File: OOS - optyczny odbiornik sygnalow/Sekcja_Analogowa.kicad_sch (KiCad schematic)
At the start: 52 parts, among them J1 Conn_01x02_Socket, J2 Conn_01x02_Socket, J3 Conn_01x02_Socket, J4 Conn_01x02_Socket, J5 Conn_Coaxial, U1 OPA300AIDBVR, U2 OPA300AIDBVR

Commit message: Finish Li-Lion section, add for review
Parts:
- removed D1, D2: LED, Diode_SMD:D_0603_1608Metric_Pad1.05x0.95mm_HandSolder, symbol Device:LED
- removed J1, J2, J3: Conn_01x02_Socket, Connector_PinHeader_2.54mm:PinHeader_1x02_P2.54mm_Vertical, symbol Connector:Conn_01x02_Socket
- removed R1: 10k, Resistor_SMD:R_0603_1608Metric_Pad0.98x0.95mm_HandSolder, symbol Device:R
- removed R2: 2k2, Resistor_SMD:R_0603_1608Metric_Pad0.98x0.95mm_HandSolder, symbol Device:R
- added TP34: TestPoint_Small, TestPoint:TestPoint_Pad_D1.0mm, symbol Connector:TestPoint_Small
- JP1: footprint Jumper:SolderJumper-2_P1.3mm_Bridged_RoundedPad1.0x1.5mm -> Jumper:SolderJumper-2_P1.3mm_Open_RoundedPad1.0x1.5mm
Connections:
- net U1/U2_En_Alt_Con: now also TP34.1
- net +5V renamed +3V3
- net +V_photo renamed +32V
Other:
- note added: "1V1"
- note added: "2V2"
- note added: "For U1_Out(max) = 10uA(Imax) * 1kR(Rf) = 10mV @ 10uA"
- note added: "Inverting amplifier x10 (1k/100)"
- note added: "changed from short to open"
- note added: "changed position 0V on schematic"
- note added: "changed value to be hidden"
- note added: "removed connectors for +V_photo, +5V and GND"
- note added: "removed indication diode from sekcja analogowa to dcdc boost"
- note removed: "+V_photo 5V to 32V"
- note removed: "1V66"
- note removed: "3V33"
- note removed: "Inverting amplifier x10 (10k/1k)"
- moved on the sheet: C1, C10, C11, C12, C2, C3, C4, C5, C6, C7, C8, C9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

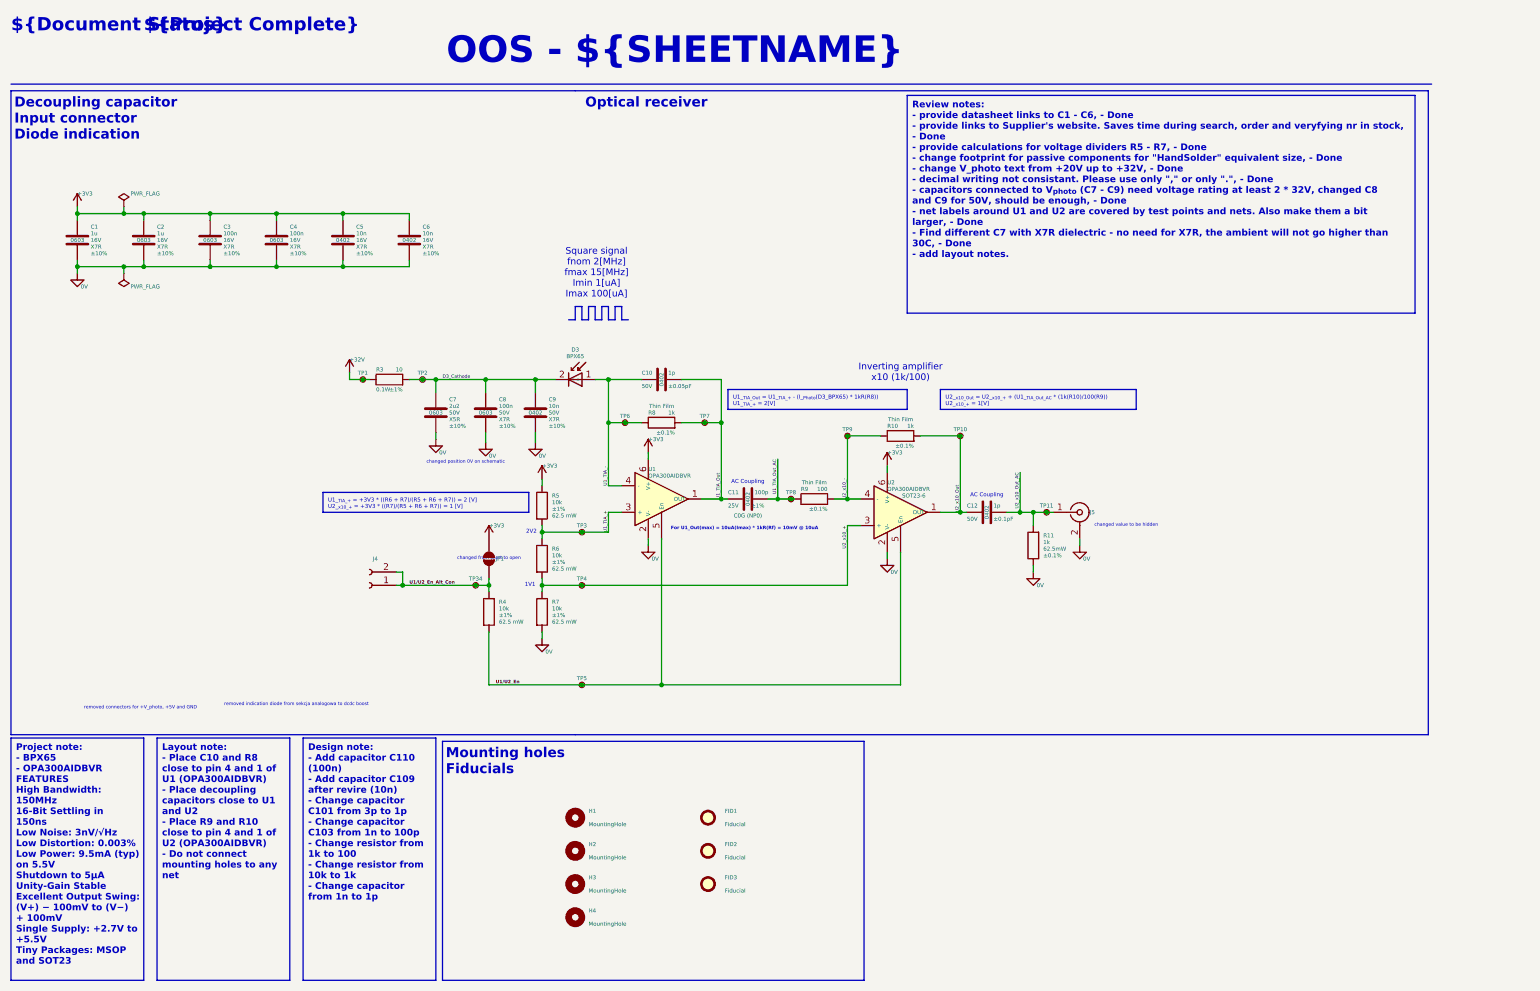
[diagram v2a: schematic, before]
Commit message: Implementing changes after review on Li-Ion section, adding components to USB section
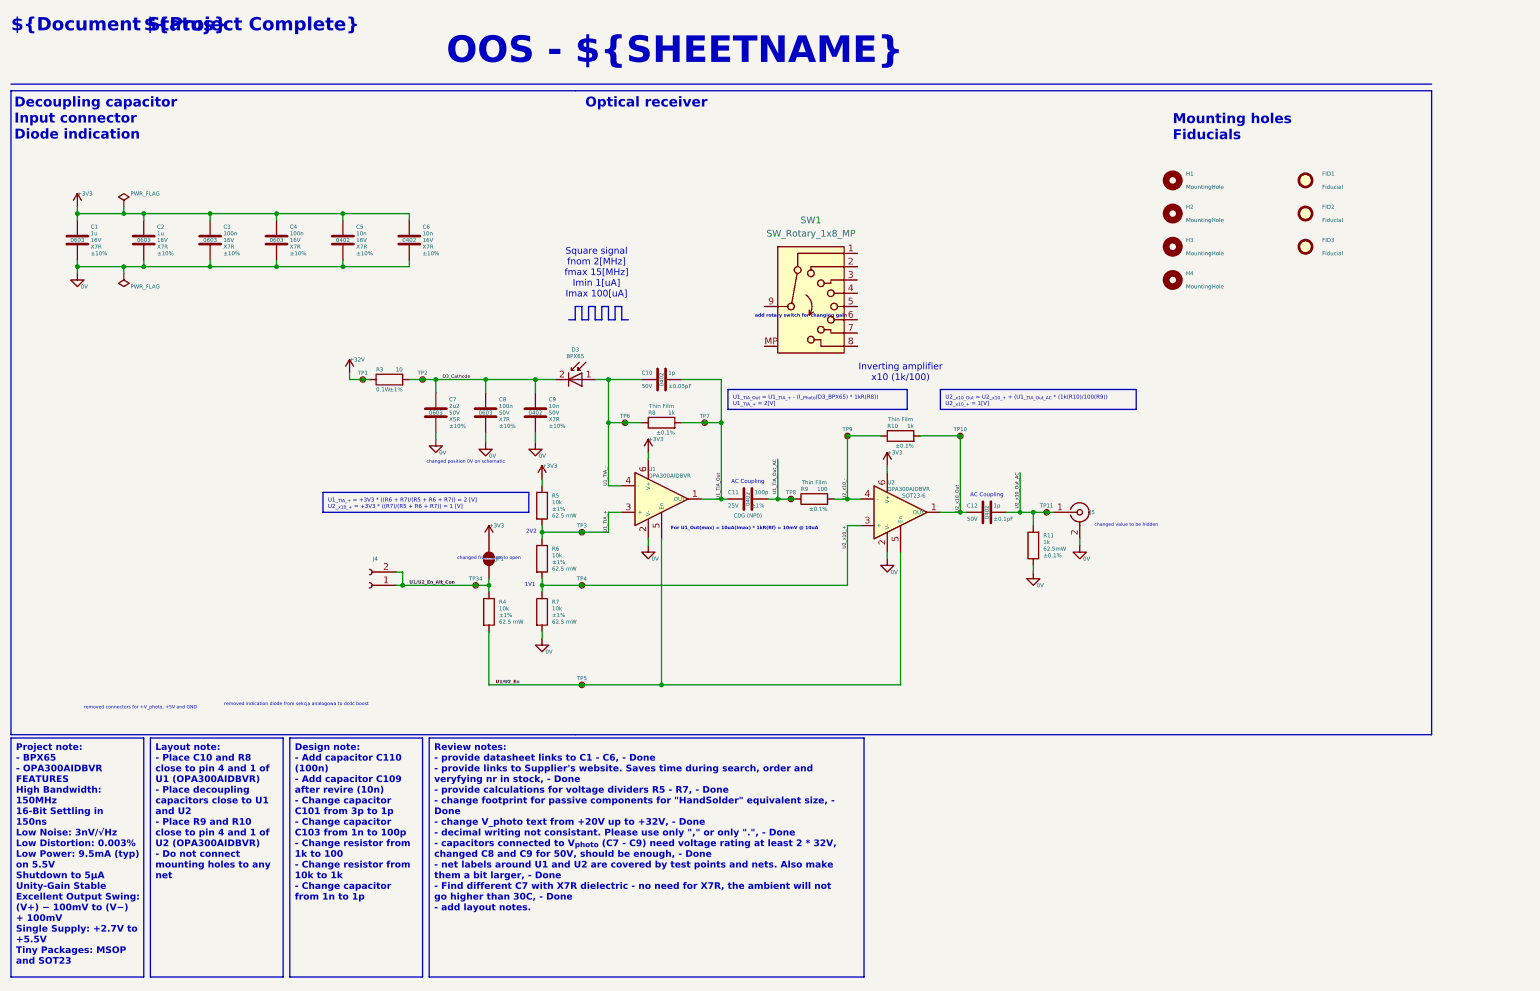
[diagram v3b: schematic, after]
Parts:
- added SW1: SW_Rotary_1x8_MP, Button_Switch_SMD:Nidec_Copal_SH-7040B, symbol Switch:SW_Rotary_1x8_MP
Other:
- note added: "add rotary switch for changing gain"
- moved on the sheet: FID1, FID2, FID3, H1, H2, H3, H4

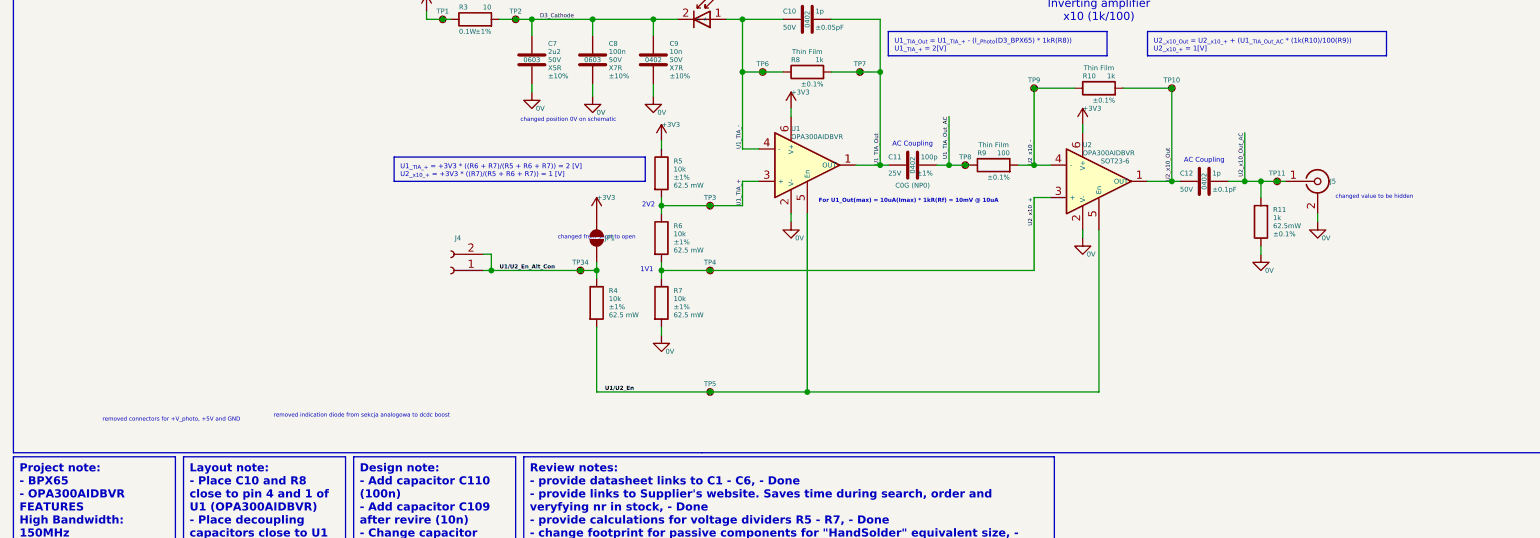
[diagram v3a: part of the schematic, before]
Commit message: Clean schematic, what left is to add resistors for pull down on usb page and rotary switch on analog page
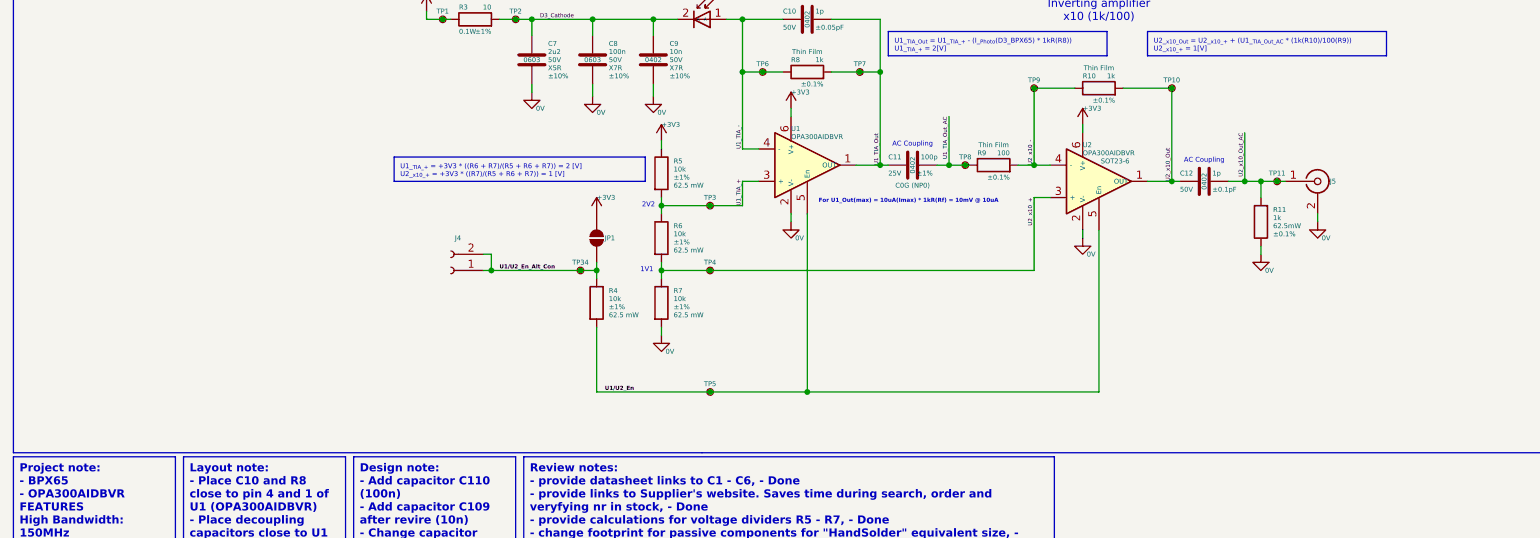
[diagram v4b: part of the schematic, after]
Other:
- note removed: "changed from short to open"
- note removed: "changed position 0V on schematic"
- note removed: "changed value to be hidden"
- note removed: "removed connectors for +V_photo, +5V and GND"
- note removed: "removed indication diode from sekcja analogowa to dcdc boost"
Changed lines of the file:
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@@
 		(comment 4 "${Project Reason}")
-	)
-	(text "removed indication diode from sekcja analogowa to dcdc boost"
-		(exclude_from_sim no)
-		(at 67.31 144.78 0)
-		(effects
-			(font
-				(size 0.635 0.635)
-				(color 255 0 0 1)
-			)
-		)
 	)
 	(text "Square signal\nfnom 2[MHz]\nfmax 15[MHz]\nImin 1[uA]\nImax 100[uA]"
@@
 				(bold yes)
 				(color 132 132 0 1)
-			)
-		)
-	)
-	(text "changed from short to open"
-		(exclude_from_sim no)
-		(at 104.14 116.84 0)
-		(effects
-			(font
-				(size 0.635 0.635)
-				(color 255 0 0 1)
 			)
 		)
@@
 		)
 	)
-	(text "changed value to be hidden"
-		(exclude_from_sim no)
-		(at 226.06 110.49 0)
-		(effects
-			(font
-				(size 0.635 0.635)
-				(color 255 0 0 1)
-			)
-		)
-	)
 	(text "${Document Status}"
 		(exclude_from_sim no)
@@
 		)
 	)
-	(text "changed position 0V on schematic"
-		(exclude_from_sim no)
-		(at 99.695 98.425 0)
-		(effects
-			(font
-				(size 0.635 0.635)
-				(color 255 0 0 1)
-			)
-		)
-	)
 	(text "2V2"
 		(exclude_from_sim no)
@@
 		)
 	)
-	(text "removed connectors for +V_photo, +5V and GND"
-		(exclude_from_sim no)
-		(at 37.465 145.415 0)
-		(effects
-			(font
-				(size 0.635 0.635)
-				(color 255 0 0 1)
-			)
-		)
-	)

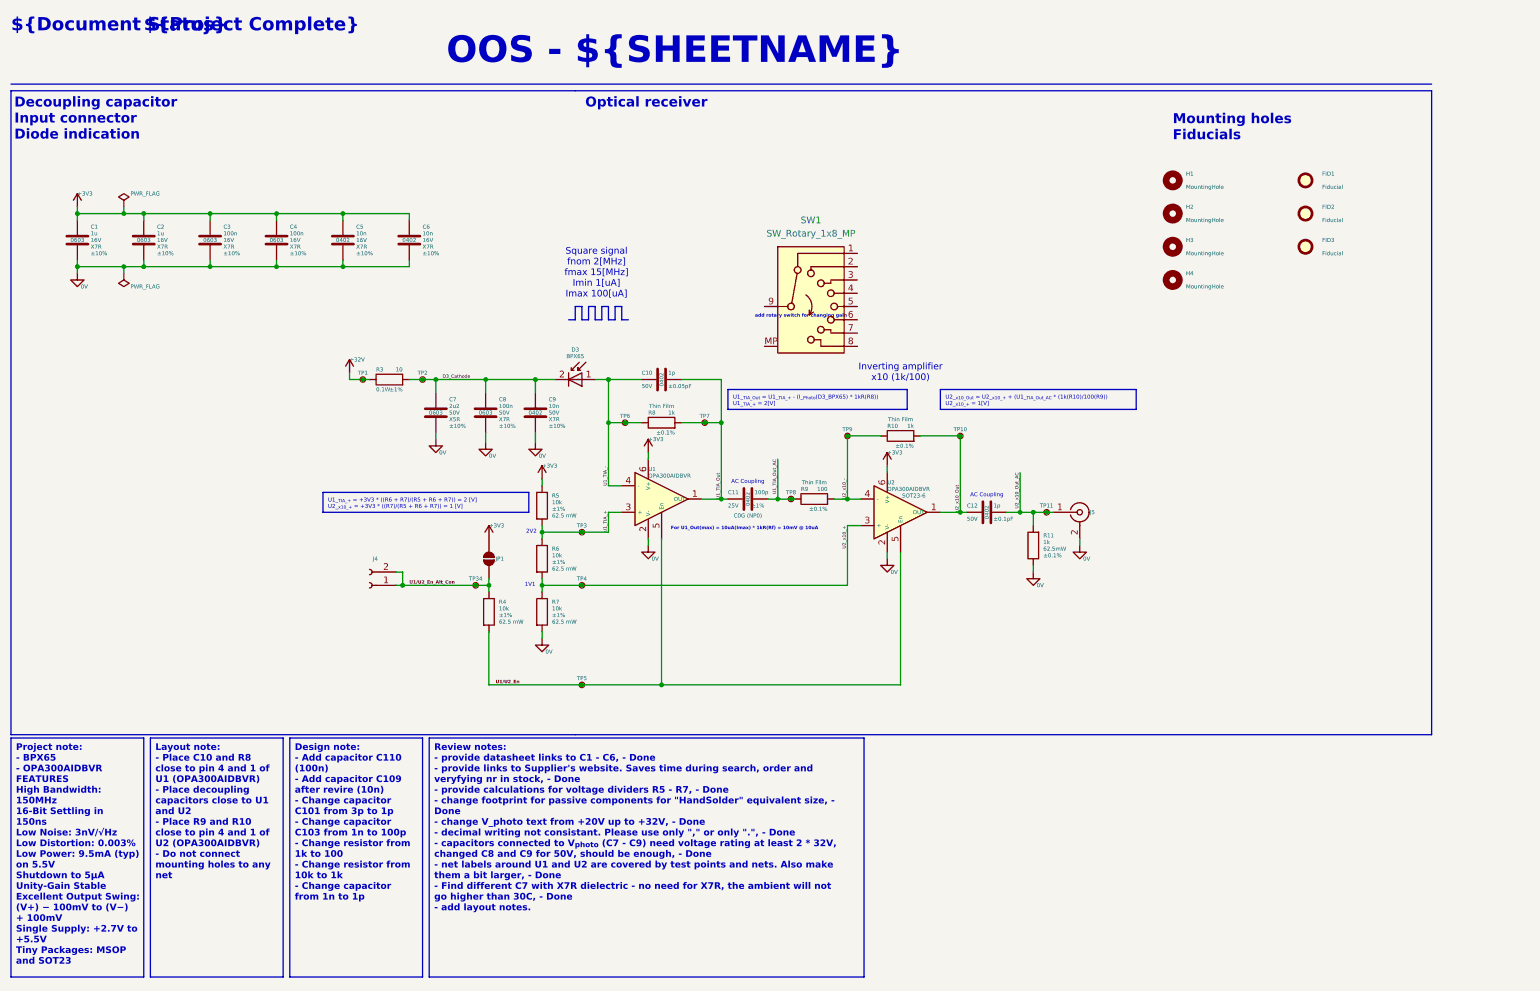
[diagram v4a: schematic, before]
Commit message: Zrobiono placement oraz routing. Nalezy jeszcze dodac przelotki do gnd blisko pinow na top layer
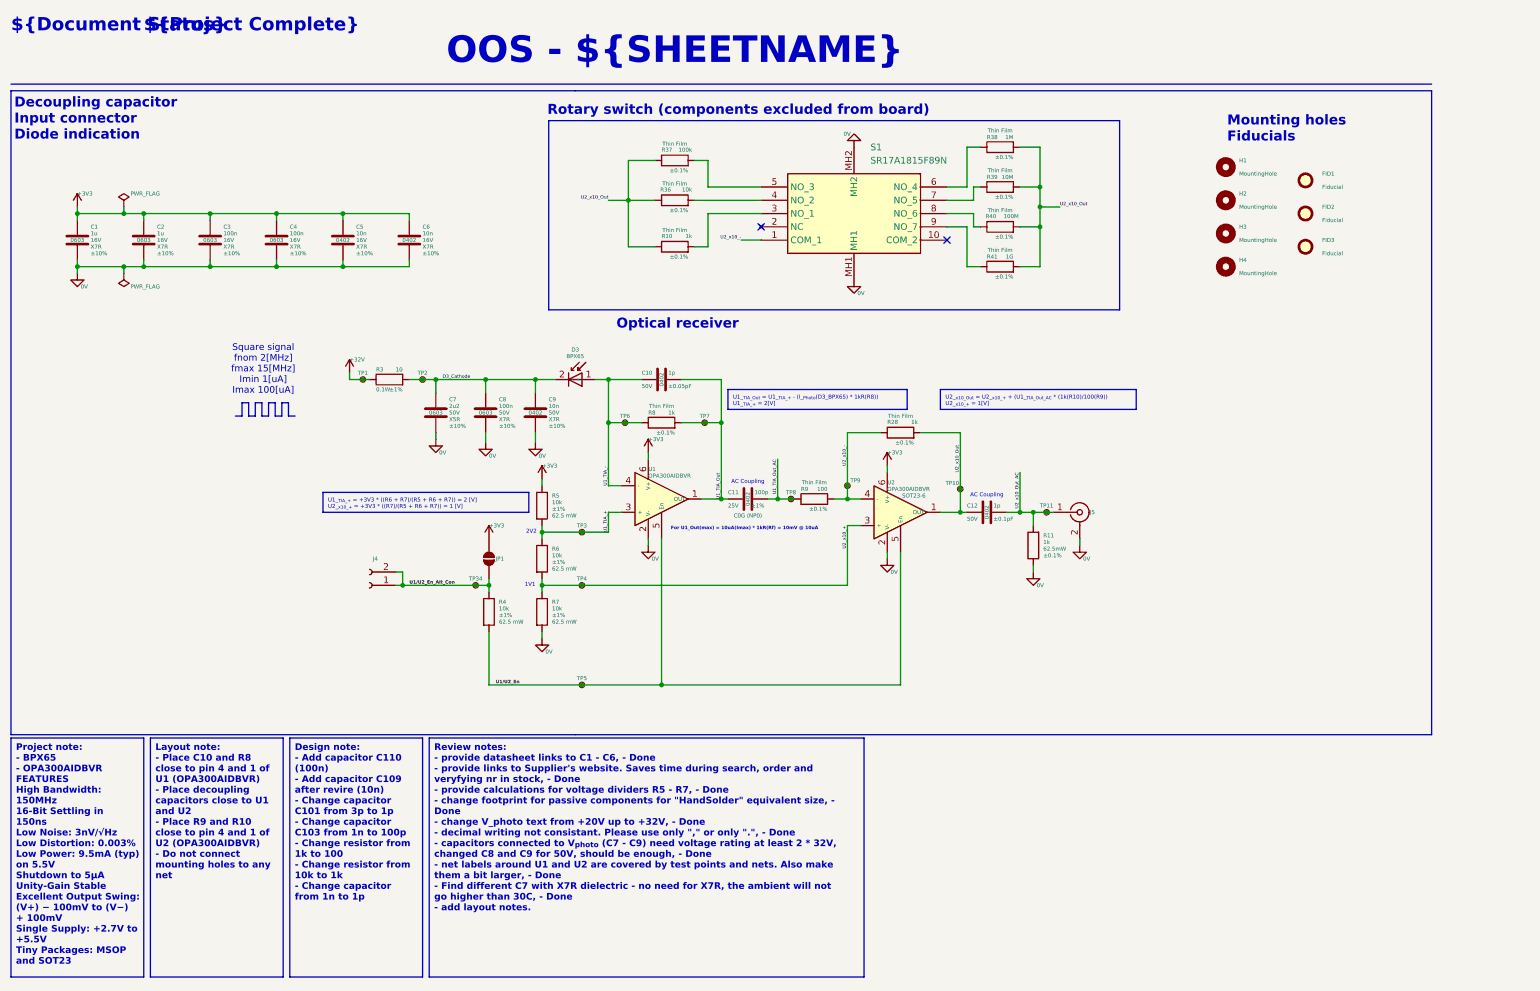
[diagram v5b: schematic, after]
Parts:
- removed SW1: SW_Rotary_1x8_MP, Button_Switch_SMD:Nidec_Copal_SH-7040B, symbol Switch:SW_Rotary_1x8_MP
- added R28: 1k, Resistor_SMD:R_0402_1005Metric_Pad0.72x0.64mm_HandSolder, symbol Device:R
- added R36: 10k, Resistor_SMD:R_0402_1005Metric_Pad0.72x0.64mm_HandSolder, symbol Device:R
- added R37: 100k, Resistor_SMD:R_0402_1005Metric_Pad0.72x0.64mm_HandSolder, symbol Device:R
- added R38: 1M, Resistor_SMD:R_0402_1005Metric_Pad0.72x0.64mm_HandSolder, symbol Device:R
- added R39: 10M, Resistor_SMD:R_0402_1005Metric_Pad0.72x0.64mm_HandSolder, symbol Device:R
- added R40: 100M, Resistor_SMD:R_0402_1005Metric_Pad0.72x0.64mm_HandSolder, symbol Device:R
- added R41: 1G, Resistor_SMD:R_0402_1005Metric_Pad0.72x0.64mm_HandSolder, symbol Device:R
- added S1: SR17A1815F89N, rotary_switch:SR17A1815F89N, symbol Rotary_switch:SR17A1815F89N
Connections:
- net 0V: now also S1.MH1, S1.MH2
- net U2_x10_-: now also R28.1, S1.1 (COM_1); no longer R10.1
- net U2_x10_Out: now also R10.1, R28.2, R36.1, R37.1, R38.2, R39.2, R40.2, R41.2; no longer R10.2
- new net: R36.2, S1.4 (NO_2)
- new net: R40.1, S1.8 (NO_6)
- new net: R10.2, S1.3 (NO_1)
- new net: R37.2, S1.5 (NO_3)
- new net: R38.1, S1.6 (NO_4)
- new net: R39.1, S1.7 (NO_5)
- new net: R41.1, S1.9 (NO_7)
- no-connect marks 0 -> 2
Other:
- note added: "Rotary switch (components excluded from board)"
- note removed: "Inverting amplifier x10 (1k/100)"
- note removed: "add rotary switch for changing gain"
- moved on the sheet: H1, H2, H3, H4, TP10
